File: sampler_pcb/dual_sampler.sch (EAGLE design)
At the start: 3 parts

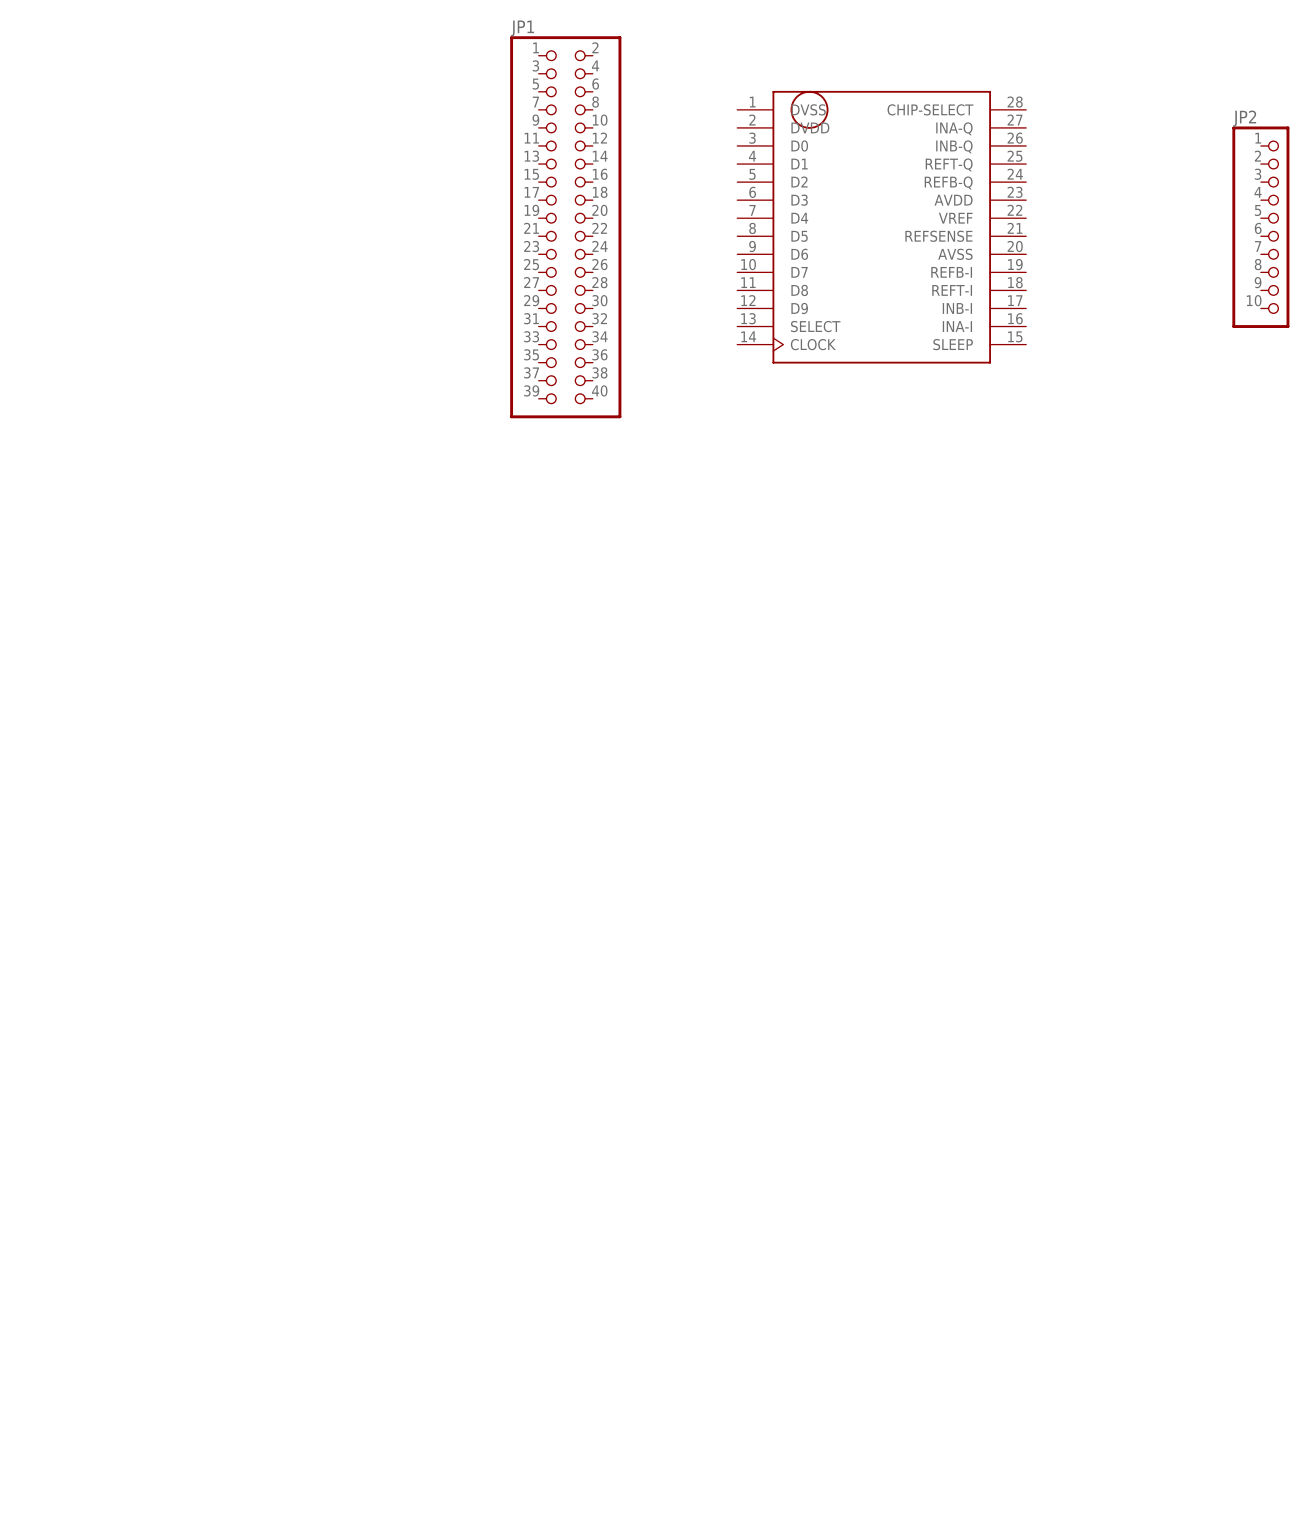
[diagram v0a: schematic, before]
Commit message: updated schematic, 1st try at board
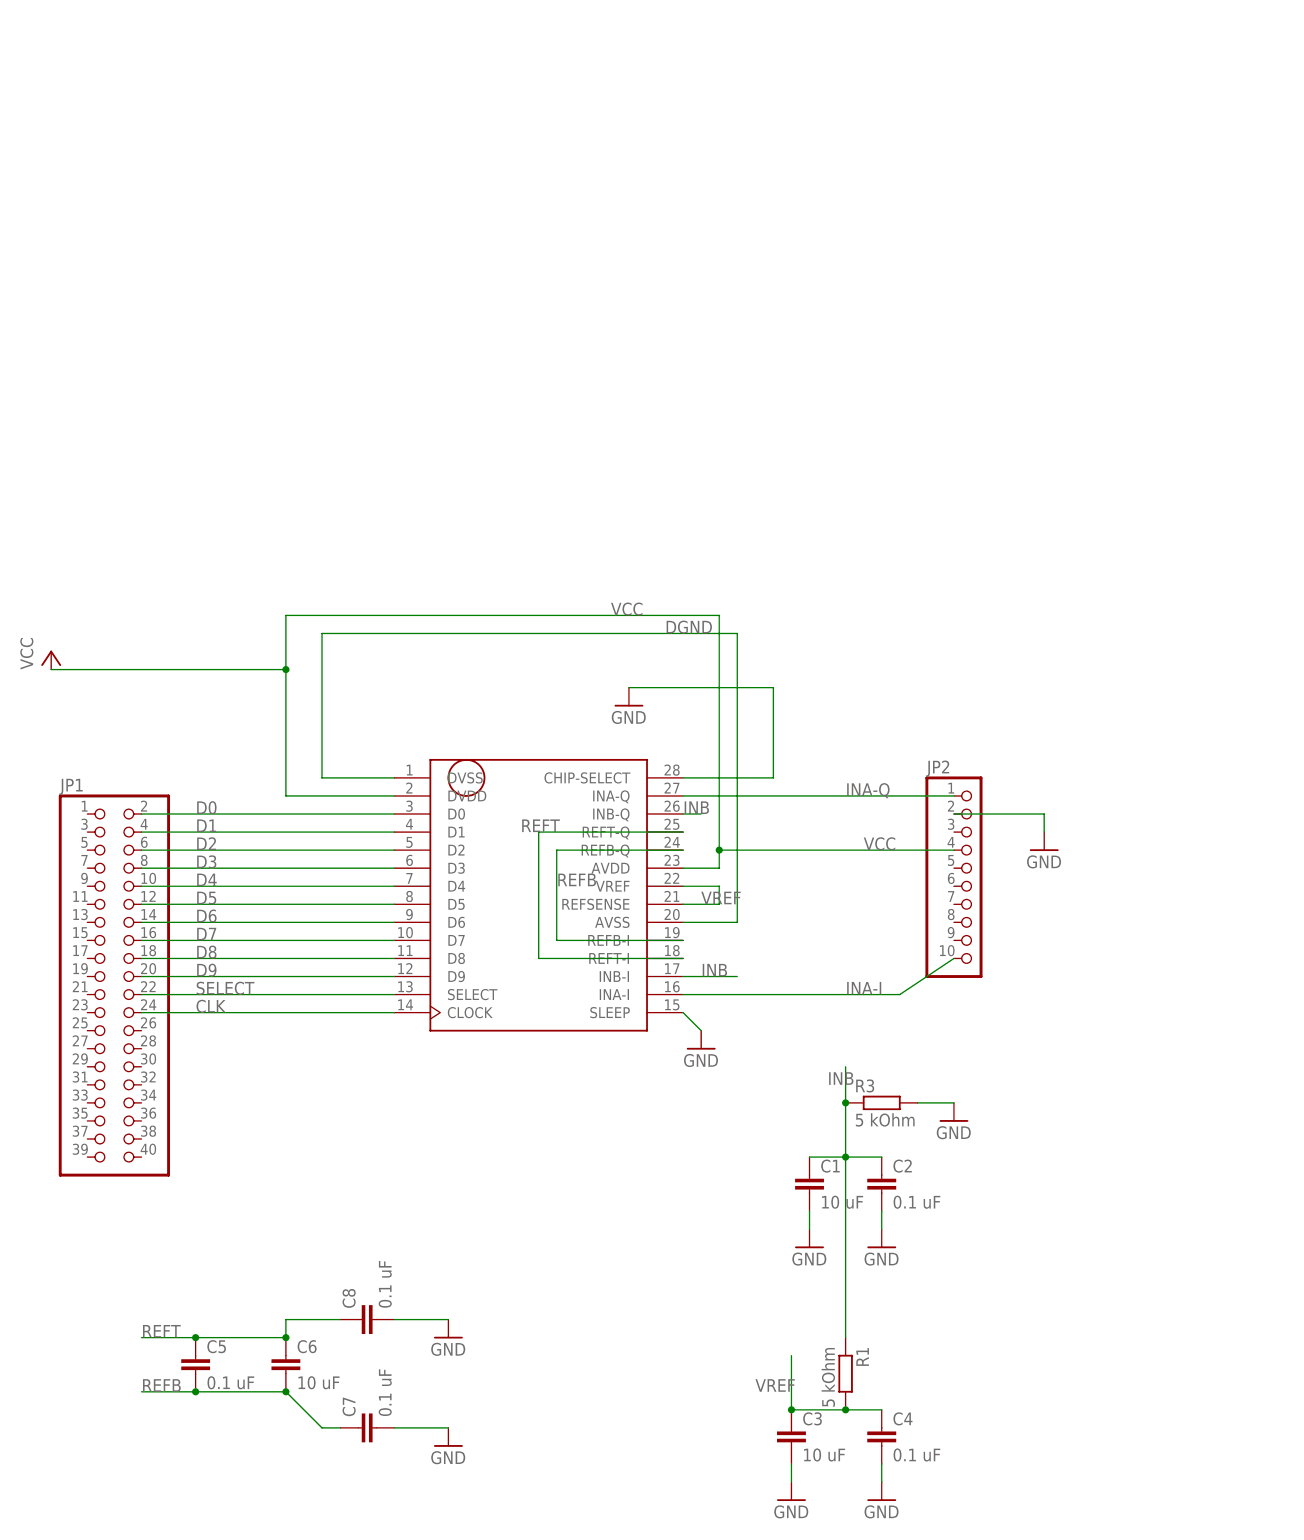
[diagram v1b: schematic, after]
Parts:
- added C1, C3, C6: 10 uF, capacitor-wima:C2,5-3
- added C2, C4, C5, C7, C8: 0.1 uF, capacitor-wima:C2,5-3
- added R1, R3: 5 kOhm, resistor:R-EU_0204/7
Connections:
- new net CLK: JP1.24, U$1.CLOCK
- new net D0: JP1.2, U$1.D0
- new net D1: JP1.4, U$1.D1
- new net D2: JP1.6, U$1.D2
- new net D3: JP1.8, U$1.D3
- new net D4: JP1.10, U$1.D4
- new net D5: JP1.12, U$1.D5
- new net D6: JP1.14, U$1.D6
- new net D7: JP1.16, U$1.D7
- new net D8: JP1.18, U$1.D8
- new net D9: JP1.20, U$1.D9
- new net DGND: U$1.AVSS, U$1.DVSS
- new net GND: C1.2, C2.2, C3.2, C4.2, C7.2, C8.2, JP2.2, R3.2, U$1.CHIP-SELECT, U$1.SLEEP
- new net INA-I: JP2.10, U$1.INA-I
- new net INA-Q: JP2.1, U$1.INA-Q
- new net INB: C1.1, C2.1, R1.1, R3.1, U$1.INB-I, U$1.INB-Q
- new net REFB: C5.2, C6.2, C7.1, U$1.REFB-I, U$1.REFB-Q
- new net REFT: C5.1, C6.1, C8.1, U$1.REFT-I, U$1.REFT-Q
- new net SELECT: JP1.22, U$1.SELECT
- new net VCC: JP2.4, U$1.AVDD, U$1.DVDD
- new net VREF: C3.1, C4.1, R1.2, U$1.REFSENSE, U$1.VREF
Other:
- moved on the sheet: JP1, JP2
